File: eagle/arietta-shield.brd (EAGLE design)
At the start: 101.6 x 53.3 mm, 13 parts

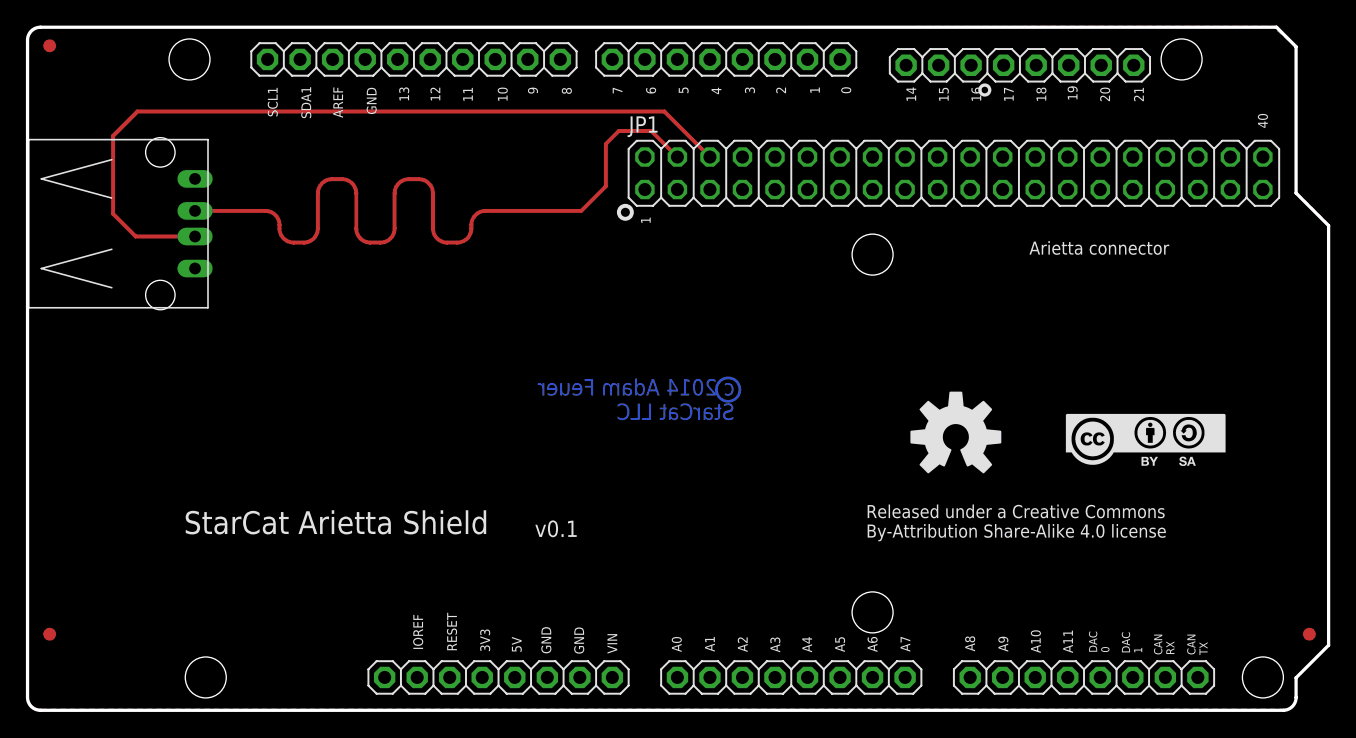
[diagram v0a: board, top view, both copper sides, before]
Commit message: added unpopulated SPI and rear connectors
- 5V now only connected to USB now, not shield connector,
  enabling connection to another computer when connected to
  the Arduino Due
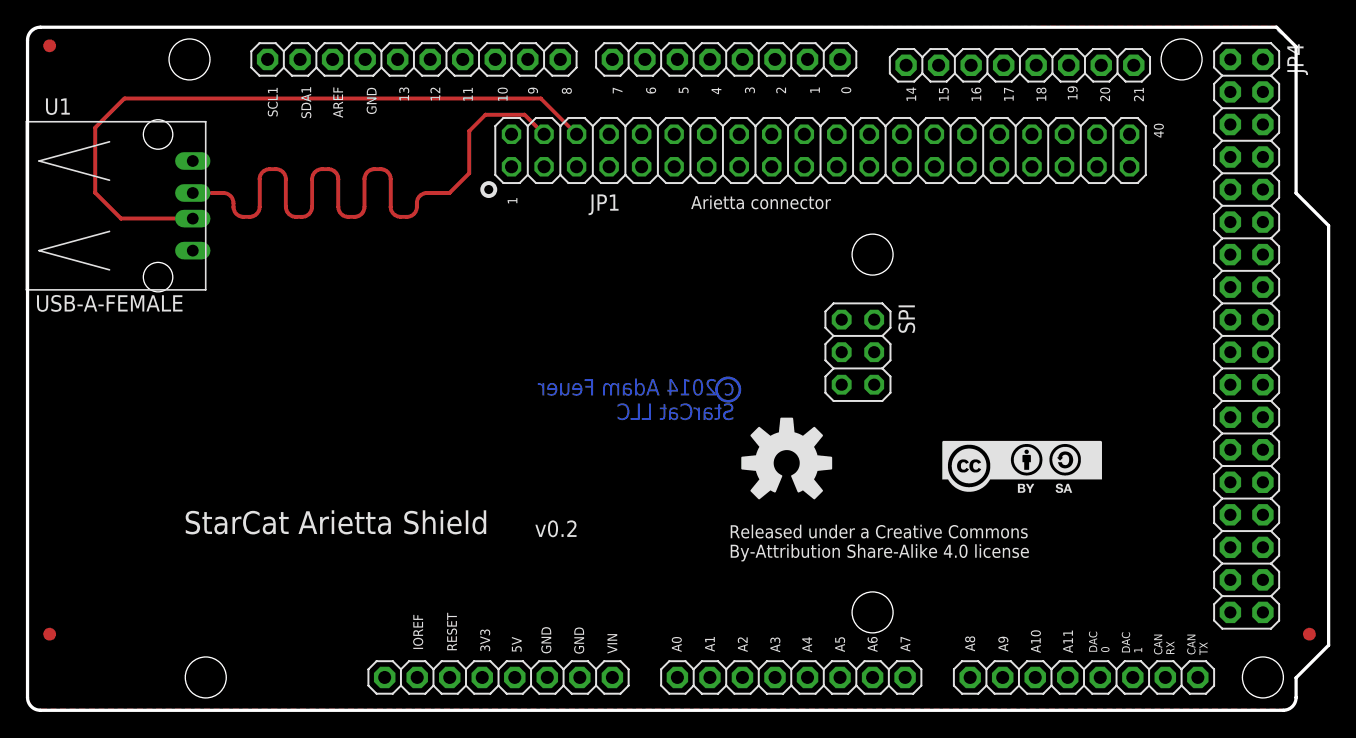
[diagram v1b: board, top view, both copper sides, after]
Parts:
- removed U$7: USB-A-FEMALE, te-conn-usb:USB-A-FEMALE
- added JP4: XIO, SmartPrj:2X18
- added SPI: SPI, SmartPrj:2X03
- added U1: USB-A-FEMALE, te-conn-usb:USB-A-FEMALE
- moved U$1 13.4 mm to (59.3, 19.3)
- moved JP1 10.6 mm to (62.0, 43.7)
- moved U$8 9.88 mm to (71.4, 16.7)
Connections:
- new net D38: JP4.19
- new net D39: JP4.20
- new net D40: JP4.21
- new net D41: JP4.22
- new net D42: JP4.23
- new net D43: JP4.24
- new net D44: JP4.25
- new net D45: JP4.26
- new net N$109: JP4.31
- new net N$115: JP4.1
- new net N$116: JP4.2
- new net N$580: JP4.5
- new net N$581: JP4.7
- new net N$582: JP4.11
- new net N$583: JP4.13
- new net N$584: JP4.27
- new net N$585: JP4.29
- new net N$586: JP4.33
- new net N$587: JP4.4
- new net N$588: JP4.6
- new net N$589: JP4.8
- new net N$590: JP4.12
- new net N$591: JP4.14
- new net N$592: JP4.30
- new net N$601: JP4.28
- new net N$73: JP4.34
- new net N$74: JP4.32
- new net N$89: JP4.18
- new net N$91: JP4.16
- new net N$92: JP4.10
- new net N$93: JP4.3
- new net N$94: JP4.9
- new net N$96: JP4.15
- new net N$97: JP4.17
- new net RESET: SPI.5
- new net SPI0_MISO: SPI.1
- new net SPI0_MOSI: SPI.4
- new net SPI0_SCK: SPI.3
- new net VCC_5V: SPI.2
- net 5V: now also U1.5V; no longer JP15.5, U$7.5V
- net D_N: now also U1.D_N; no longer U$7.D_N
- net D_P: now also U1.D_P; no longer U$7.D_P
- net GND: now also JP4.35, JP4.36, SPI.6, U1.GND; no longer U$7.GND
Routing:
- net D_P: track 62.1 -> 53.2 mm
- net D_N: track 60.0 -> 51.3 mm
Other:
- board text added: "v0.2"
- board text removed: "v0.1"
